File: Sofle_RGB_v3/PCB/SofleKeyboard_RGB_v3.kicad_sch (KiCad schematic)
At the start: 98 parts, among them J1 LED, J2 4PIN, J3 OLED, J4 key leds, J5 backlight sel, J6 indicator bypass, J7 BAT, P1 i2c_pin, P2 i2c_pin, SW1 SW_PUSH-MX_W_LED, SW10 SW_PUSH-MX_W_LED, SW11 SW_PUSH-MX_W_LED, SW12 SW_PUSH-MX_W_LED, SW13 SW_PUSH-MX_W_LED, SW14 SW_PUSH-MX_W_LED, SW15 SW_PUSH-MX_W_LED, SW16 SW_PUSH-MX_W_LED, SW17 SW_PUSH-MX_W_LED, SW18 SW_PUSH-MX_W_LED, SW19 SW_PUSH-MX_W_LED, SW2 SW_PUSH-MX_W_LED, SW20 SW_PUSH-MX_W_LED, SW21 SW_PUSH-MX_W_LED, SW22 SW_PUSH-MX_W_LED, SW23 SW_PUSH-MX_W_LED, SW24 SW_PUSH-MX_W_LED, SW25 Rotary_Encoder_Switch, SW26 SW_PUSH-MX_W_LED, SW27 SW_PUSH-MX_W_LED, SW28 SW_PUSH-MX_W_LED, SW29 SW_PUSH-MX_W_LED, SW3 SW_PUSH-MX_W_LED, SW30 SW_PUSH-MX_W_LED, SW31 PWR Top, SW32 PWR Bottom, SW4 SW_PUSH-MX_W_LED, SW5 SW_PUSH-MX_W_LED, SW6 SW_PUSH-MX_W_LED, SW7 SW_PUSH-MX_W_LED, SW8 SW_PUSH-MX_W_LED, SW9 SW_PUSH-MX_W_LED, U1 ProMicro

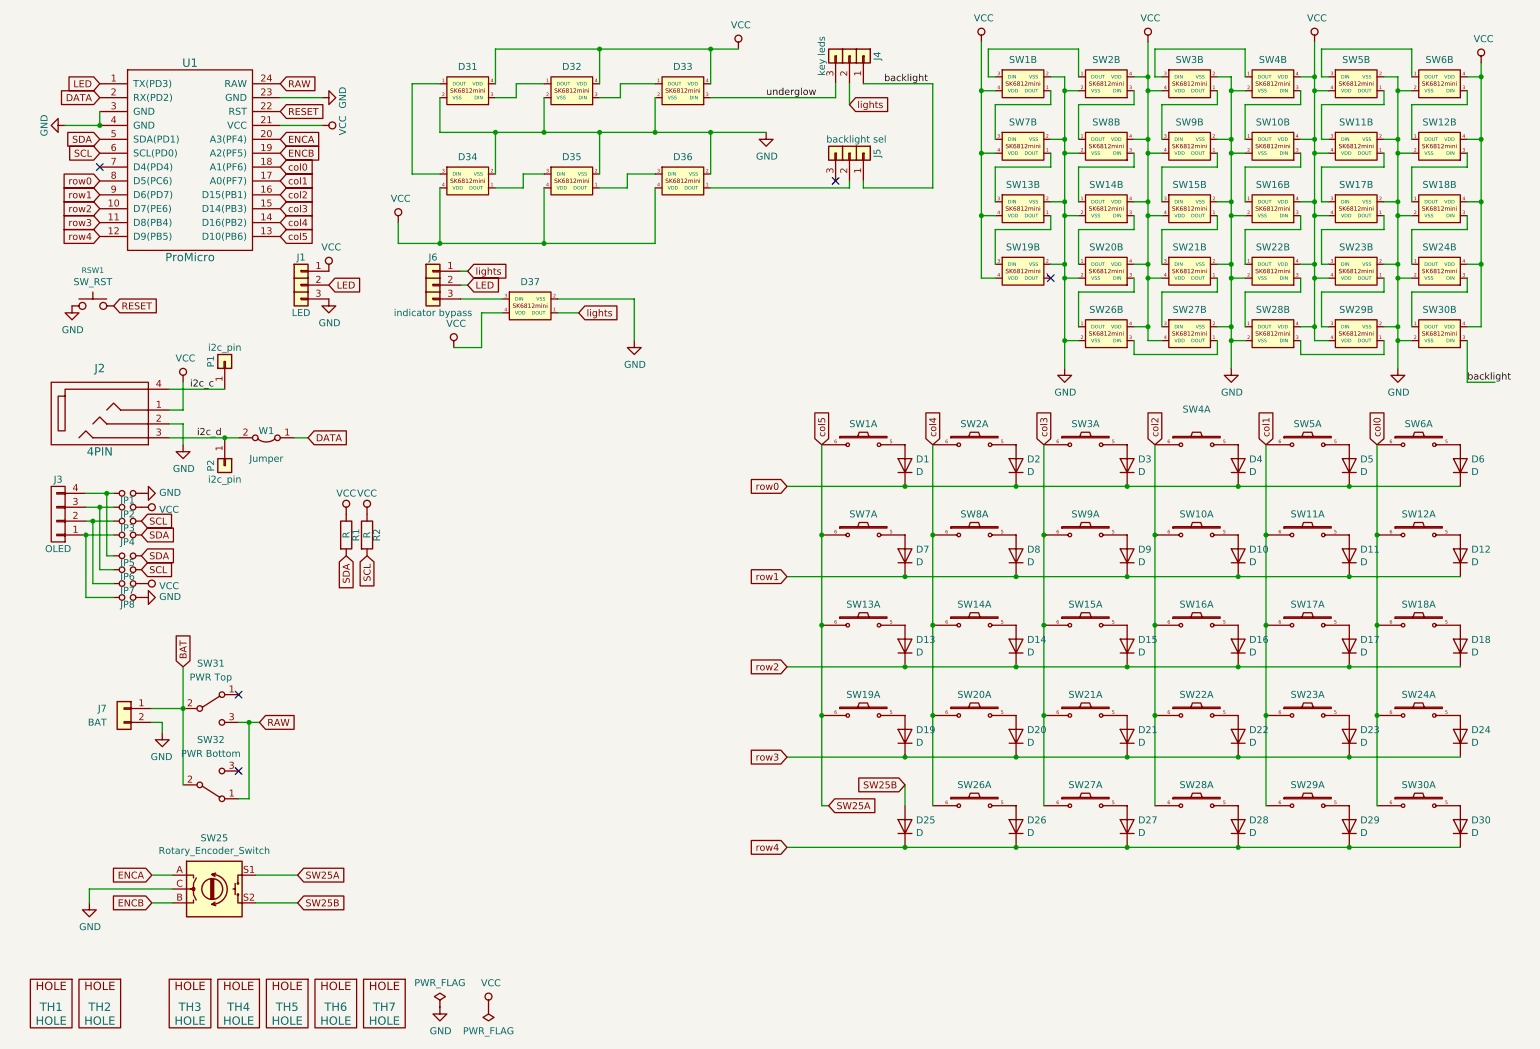
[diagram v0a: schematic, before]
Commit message: Sofle RGB V3.2 with native nice!view support
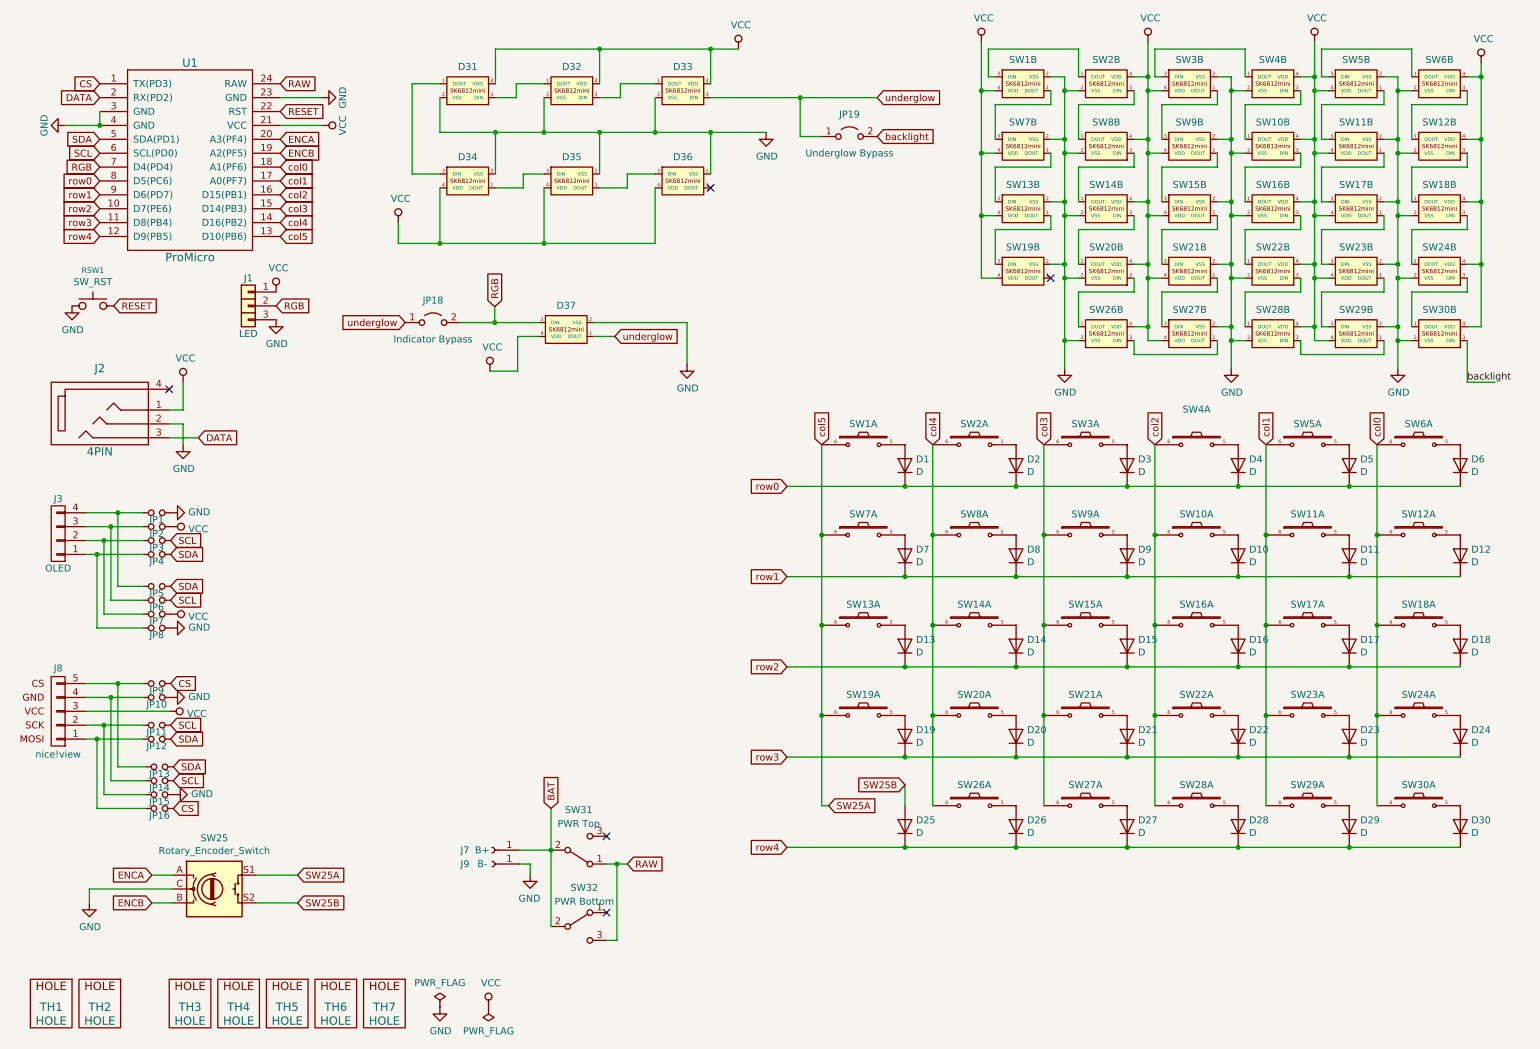
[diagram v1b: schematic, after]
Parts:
- removed J4: key leds, Connector:3x1header, symbol SofleKeyboard-rescue:LED-Lily58-cache-Lily58_Pro-rescue
- removed J5: backlight sel, Connector:3x1header, symbol SofleKeyboard-rescue:LED-Lily58-cache-Lily58_Pro-rescue
- removed J6: indicator bypass, Connector:3x1header, symbol SofleKeyboard-rescue:LED-Lily58-cache-Lily58_Pro-rescue
- removed J7: BAT, Connector_PinHeader_2.54mm:PinHeader_1x02_P2.54mm_Vertical, symbol Connector_Generic:Conn_01x02
- removed P1, P2: i2c_pin, SofleKeyboard-footprint:1pin_conn, symbol SofleKeyboard-rescue:i2c_pin-Lily58-cache-Lily58_Pro-rescue
- removed R1, R2: R, SofleKeyboard-footprint:RESISTOR_mini, symbol SofleKeyboard-rescue:R-Lily58-cache-Lily58_Pro-rescue
- removed W1: Jumper, Jumper:SolderJumper-2_P1.3mm_Bridged_RoundedPad1.0x1.5mm, symbol Jumper:Jumper_2_Bridged
- added J7: B+, SofleKeyboard-footprint:1pin_conn, symbol Connector:Conn_01x01_Female
- added J8: nice!view, SofleKeyboard-footprint:niceview_5Pin, symbol SofleKeyboard-rescue:niceview-Lily58-cache-Lily58_Pro-rescue
- added J9: B-, SofleKeyboard-footprint:1pin_conn, symbol Connector:Conn_01x01_Female
- added JP10, JP11, JP12, JP13, JP14, JP15, JP16, JP9: Jumper_NO_Small, SofleKeyboard-footprint:Jumper, symbol SofleKeyboard-rescue:Jumper_NO_Small-Device
- added JP18: Indicator Bypass, Jumper:SolderJumper-2_P1.3mm_Open_TrianglePad1.0x1.5mm, symbol Jumper:Jumper_2_Open
- added JP19: Underglow Bypass, Jumper:SolderJumper-2_P1.3mm_Open_TrianglePad1.0x1.5mm, symbol Jumper:Jumper_2_Open
- D1, D10, D11, D12, D13, D14, D15, D16, D17, D18, D19, D2, D20, D21, D22, D23, D24, D25, D26, D27, D28, D29, D3, D30, D4, D5, D6, D7, D8, D9: footprint Diode_SMD:crkbd-diode -> SofleKeyboard-footprint:SOD-223_with_cutout
- D31, D32, D33, D34, D35, D36, D37: footprint LED_SMD:SK6812MINI_underglow_dev -> SofleKeyboard-footprint:SK6812MINI_underglow_with_cutout
- J2: footprint SofleKeyboard-footprint:MJ-4PP-9 -> SofleKeyboard-footprint:PJ-320A_double_sided_with_cutouts
- SW1, SW10, SW11, SW12, SW13, SW14, SW15, SW16, SW17, SW18, SW19, SW2, SW20, SW21, SW22, SW23, SW24, SW26, SW27, SW28, SW29, SW3, SW30, SW4, SW5, SW6, SW7, SW8, SW9: footprint Button_Switch_Keyboard:SK6812MINI_and_cherry -> SofleKeyboard-footprint:SK6812MINI_and_cherry_with_cutouts
- SW25: footprint SofleKeyboard-footprint:RotaryEncoder_Alps_EC11E-Switch_Vertical_H20mm-keebio_modified -> SofleKeyboard-footprint:RotaryEncoder_Alps_EC11E-Switch_Vertical_H20mm-keebio_modified_with_cutouts
- U1: footprint SofleKeyboard-footprint:ProMicro -> SofleKeyboard-footprint:ProMicro_with_cutouts
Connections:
- net i2c_d is gone; now on net DATA: J2.3
- net lights is gone; now on net underglow: D37.1 (DOUT)
- net BAT: now also J7.1 (Pin_1)
- net GND: now also J9.1 (Pin_1), JP10.2, JP15.2
- net RAW: now also SW31.1 (A), SW32.3 (C); no longer SW31.3 (C), SW32.1 (A)
- net SCL: now also JP11.2, JP14.2
- net SDA: now also JP12.2, JP13.2
- net VCC: now also J8.3 (P3)
- net backlight: now also JP19.2 (B)
- net underglow: now also JP18.1 (A), JP19.1 (A)
- net RGB: now reaches U1.7 (D4(PD4))
- net RGB: now also D37.3 (DIN), J1.2 (Pin_2), JP18.2 (B)
- net LED renamed CS
- net CS: now also JP16.2, JP9.2; no longer J1.2 (Pin_2)
- net i2c_c: no longer names the net of J2.4
- new net: J8.2 (P2), JP11.1, JP15.1
- new net: J8.5 (P5), JP13.1, JP9.1
- new net: J8.1 (P1), JP12.1, JP16.1
- new net: J8.4 (P4), JP10.1, JP14.1
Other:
- moved on the sheet: D37, J1, J3, JP1, JP2, JP3, JP4, JP5, JP6, JP7, JP8, SW31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

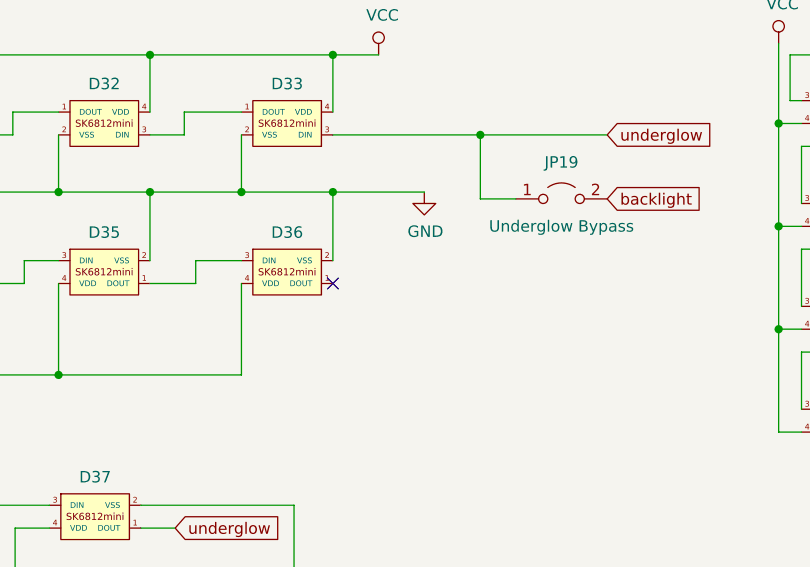
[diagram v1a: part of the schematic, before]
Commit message: Sofle RGB V3.4
* Fix missing connection between underglow and backlight
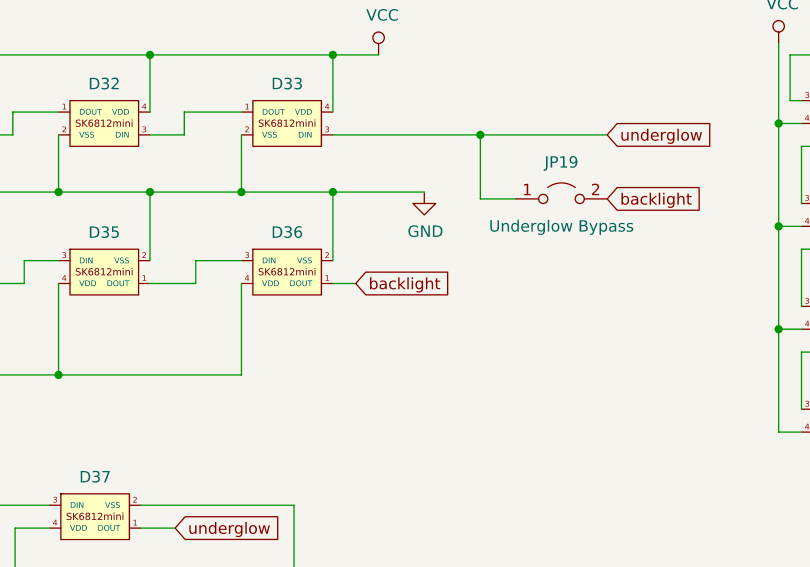
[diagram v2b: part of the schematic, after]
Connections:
- net backlight: now also D36.1 (DOUT)
- no-connect marks 5 -> 4
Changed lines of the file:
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@@
 	)
 	(no_connect
-		(at 139.7 40.64)
-	)
-	(no_connect
 		(at 40.64 77.47)
 	)
@@
 	(wire
 		(pts
+			(xy 139.7 40.64) (xy 142.24 40.64)
+		)
+		(stroke
+			(width 0)
+			(type default)
+		)
+	)
+	(wire
+		(pts
 			(xy 236.22 144.78) (xy 256.54 144.78)
 		)
@@
 			(effects
 				(font
+					(size 1.27 1.27)
+				)
+				(justify left)
+				(hide yes)
+			)
+		)
+	)
+	(global_label "backlight"
+		(shape input)
+		(at 142.24 40.64 0)
+		(fields_autoplaced yes)
+		(effects
+			(font
+				(size 1.27 1.27)
+			)
+			(justify left)
+		)
+		(property "Intersheetrefs" "${INTERSHEET_REFS}"
+			(at 153.2728 40.5606 0)
+			(effects
+				(font
